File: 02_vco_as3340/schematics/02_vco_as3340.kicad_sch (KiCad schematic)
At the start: 52 parts, among them U1 AS3340, U2 TL074, U3 TL074

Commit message: worked on  02_vco_as3340 schematics
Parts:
- removed C2: 1nF, Capacitor_THT:C_Disc_D6.0mm_W2.5mm_P5.00mm, symbol Device:C_Small
- removed R16, R27: 1k, Resistor_THT:R_Axial_DIN0207_L6.3mm_D2.5mm_P10.16mm_Horizontal, symbol Device:R_Small
- removed R19, R20, R21: 47k, Resistor_THT:R_Axial_DIN0207_L6.3mm_D2.5mm_P10.16mm_Horizontal, symbol Device:R_Small
- removed R22: 2k, Resistor_THT:R_Axial_DIN0207_L6.3mm_D2.5mm_P10.16mm_Horizontal, symbol Device:R_Small
- removed R28, R29, R33, R6: 100k, Resistor_THT:R_Axial_DIN0207_L6.3mm_D2.5mm_P10.16mm_Horizontal, symbol Device:R_Small
- removed RV5: 100k, Potentiometer_THT:Potentiometer_Alpha_RD901F-40-00D_Single_Vertical_CircularHoles, symbol Device:R_Potentiometer_Small
- removed TP2: 10k, Potentiometer_THT:Potentiometer_Vishay_T73XW_Horizontal, symbol Device:R_Potentiometer_Trim
- removed unit 3 of U2
- removed unit 2 of U2
- removed unit 4 of U3
- removed unit 3 of U3
- removed ZD1: 10V Zener Diode, symbol Device:D_Zener_Small
- added C1001: 1nF, Capacitor_THT:C_Disc_D6.0mm_W2.5mm_P5.00mm, symbol Device:C_Small
- added R1001: 1k, Resistor_THT:R_Axial_DIN0207_L6.3mm_D2.5mm_P10.16mm_Horizontal, symbol Device:R_Small
- added R1002, R1009: 33k, Resistor_THT:R_Axial_DIN0207_L6.3mm_D2.5mm_P10.16mm_Horizontal, symbol Device:R_Small
- added R1003: 150k, Resistor_THT:R_Axial_DIN0207_L6.3mm_D2.5mm_P10.16mm_Horizontal, symbol Device:R_Small
- added R1004: 15k, Resistor_THT:R_Axial_DIN0207_L6.3mm_D2.5mm_P10.16mm_Horizontal, symbol Device:R_Small
- added R1005, R1007: 82k, Resistor_THT:R_Axial_DIN0207_L6.3mm_D2.5mm_P10.16mm_Horizontal, symbol Device:R_Small
- added R1006: 220k, Resistor_THT:R_Axial_DIN0207_L6.3mm_D2.5mm_P10.16mm_Horizontal, symbol Device:R_Small
- added R1008, R1010, R1011, R1012, R1014: 100k, Resistor_THT:R_Axial_DIN0207_L6.3mm_D2.5mm_P10.16mm_Horizontal, symbol Device:R_Small
- added R1013: 22k, Resistor_THT:R_Axial_DIN0207_L6.3mm_D2.5mm_P10.16mm_Horizontal, symbol Device:R_Small
- added RV1001: 100k, Potentiometer_THT:Potentiometer_Alpha_RD901F-40-00D_Single_Vertical_CircularHoles, symbol Device:R_Potentiometer_Small
- added TP1001, TP1002: 10k, Potentiometer_THT:Potentiometer_Vishay_T73XW_Horizontal, symbol Device:R_Potentiometer_Trim
- R31: value 100k -> 47k
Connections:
- net PWM is gone; now on an unnamed net: U1.5 (VPWM)
- net +12V: now also TP1.3, R1003.1, R1010.1, R1014.1; no longer TP1.1
- net -12V: now also R1006.2
- net GNDREF: now also C1001.1, R1004.2, R1009.2, R1013.2, RV1001.3; no longer RV4.3, U2.12 (+)
- net Triangle Wave OUT: now also R1001.2
- net at U2.3 (+): now also R1009.1, R1010.2
- net at U1.10 (VTO): now also R1002.2; no longer U3.5 (+)
- net at U1.11 (CAP): now also C1001.2
- net at R2.1, R23.1, R24.2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: now also TP1002.1, TP1002.2
- net at U1.4 (VP): now also R1008.1
- net at U1.8 (VSO): now also R1011.1; no longer U3.3 (+)
- net at R1.1: now also TP1002.3
- net at U3.6 (-): now also R1002.1, R1005.1; no longer U3.7
- net at R25.1, U2.1: now also R1007.2; no longer U2.2 (-)
- net at R17.1, U3.1: now also R1012.2; no longer U3.2 (-)
- net at RV4.2: now also U2.12 (+)
- net at R4.2, TP1.2: now also TP1.1; no longer TP1.3
- net PWM IN: no longer names the net of R32.1
- net PWM IN: now also RV1001.2
- new net: R1007.1, R1008.2, U2.2 (-)
- new net: R1004.1, TP1001.1
- new net: R1003.2, TP1001.2, TP1001.3, U3.5 (+)
- new net: R1001.1, R1005.2, U3.7
- new net: R1013.1, R1014.2, U3.3 (+)
- new net: R1011.2, R1012.1, U3.2 (-)
- new net: R1006.1, RV4.3
- new net PWM  CV IN: RV1001.1
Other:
- moved on the sheet: C10, C4, C5, C6, C8, C9, D1, D2, R10, R11, R12, R13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

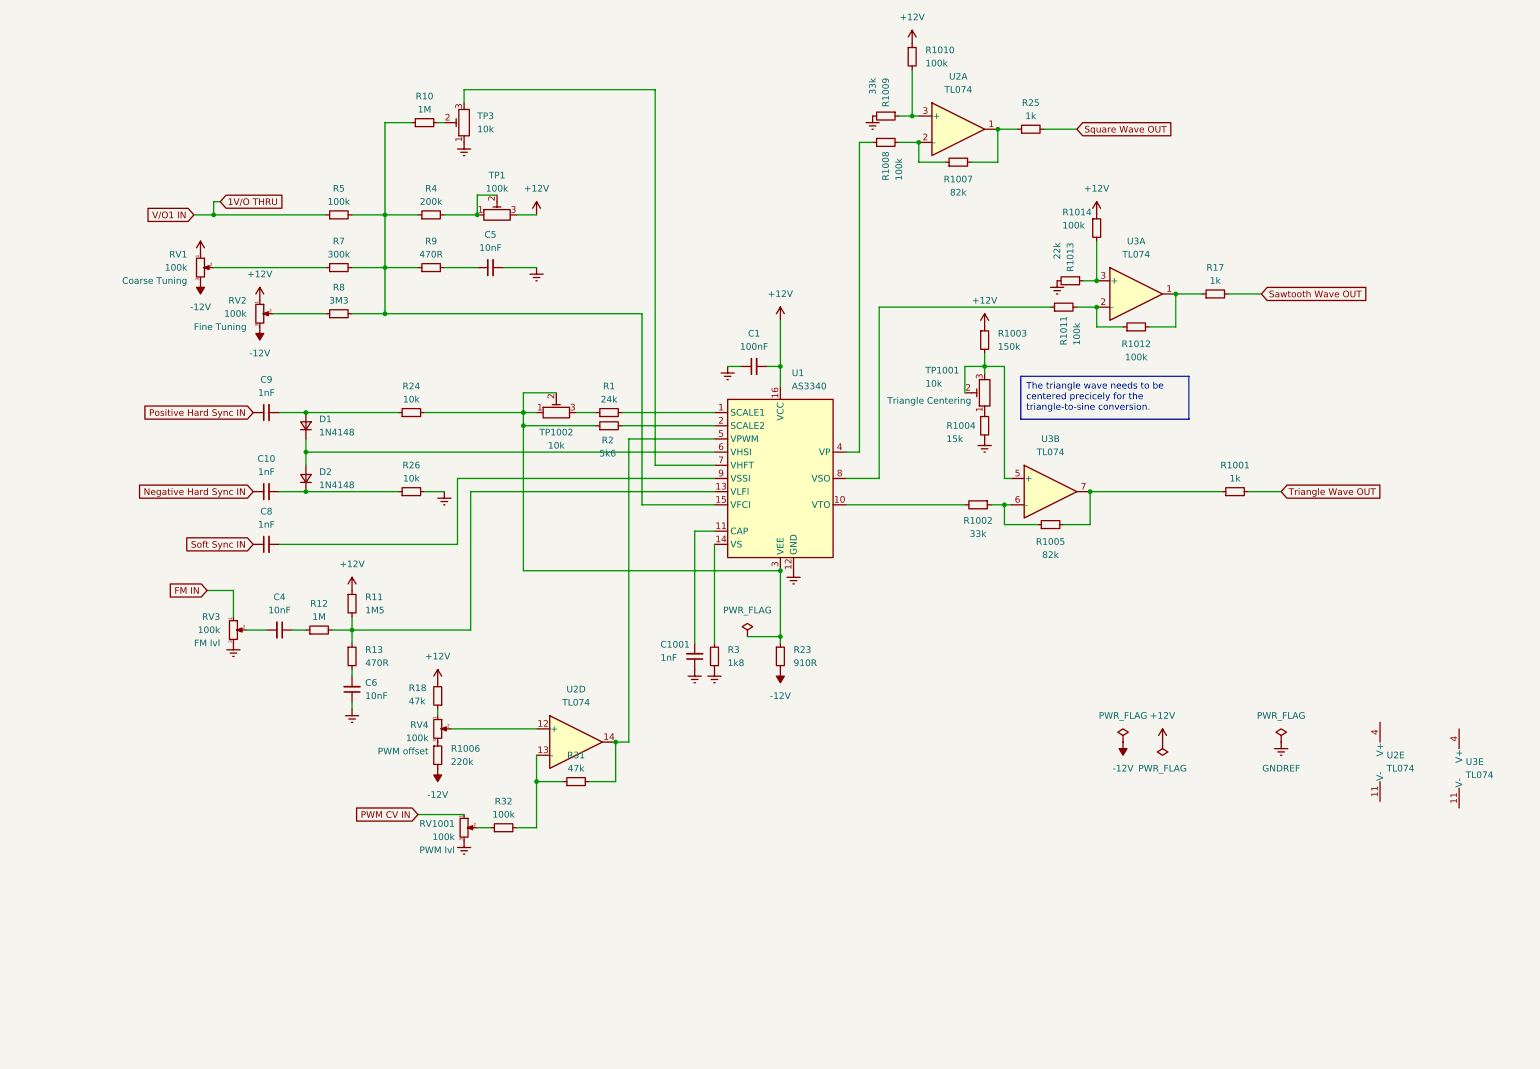
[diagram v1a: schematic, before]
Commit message: added 03_env_pluck
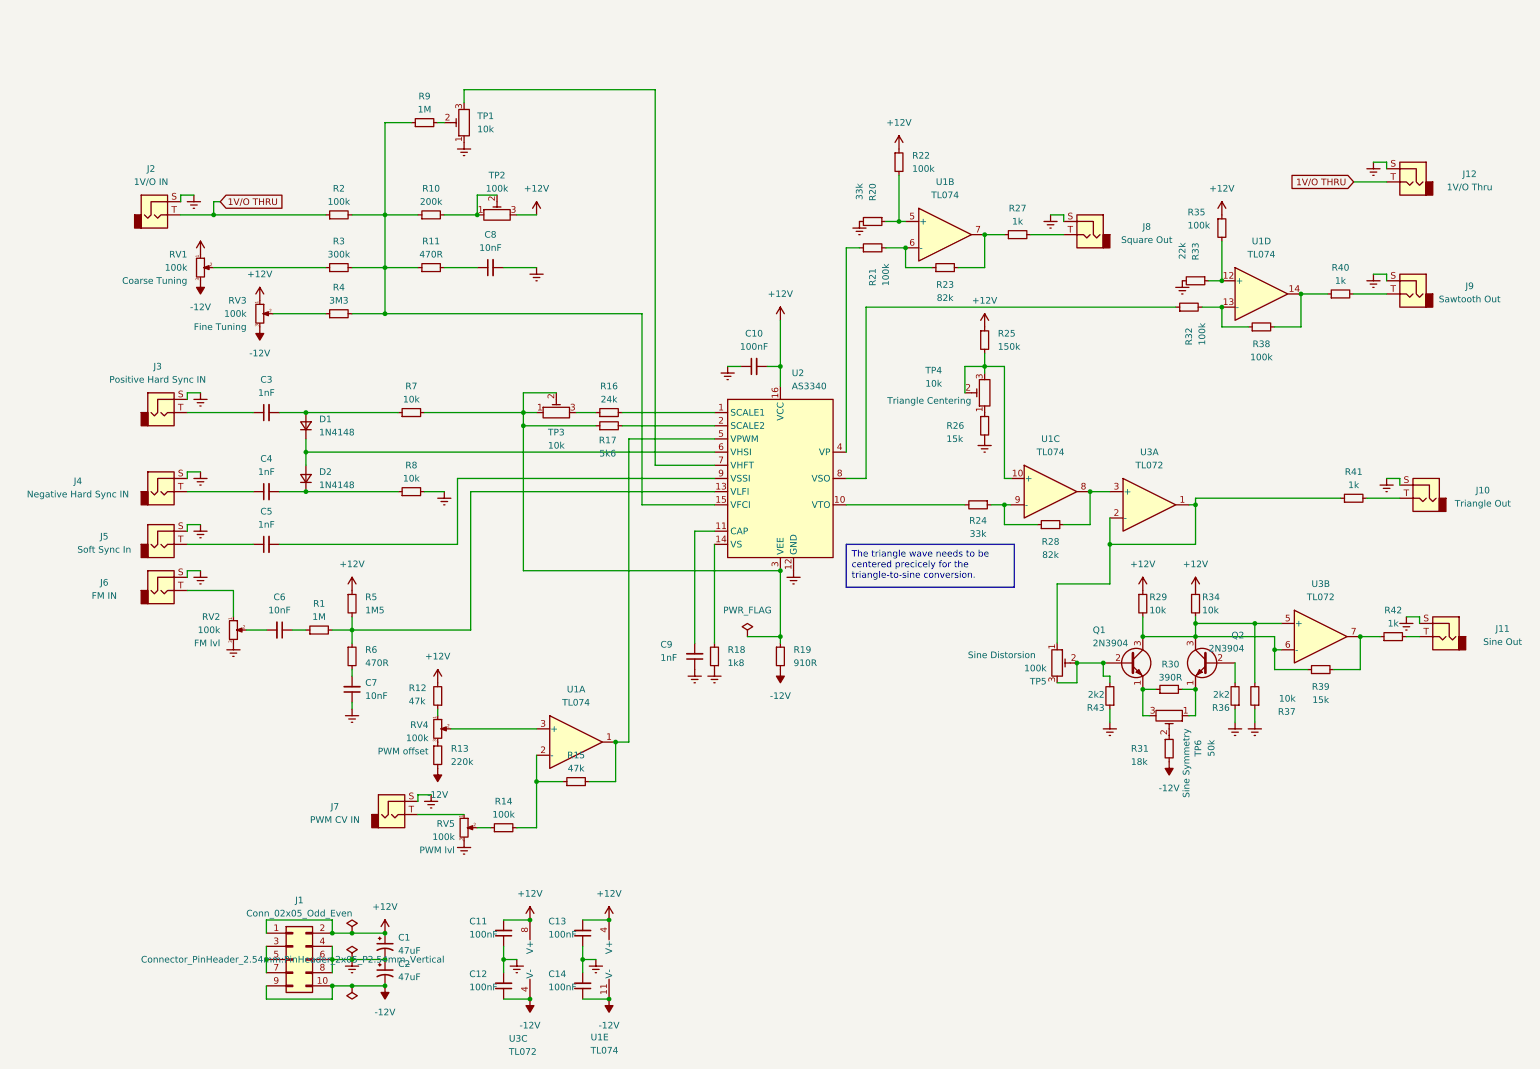
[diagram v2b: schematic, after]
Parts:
- removed U2, U3: TL074, Package_DIP:DIP-14_W7.62mm, symbol Amplifier_Operational:TL074
- added C1, C2: 47uF, Capacitor_THT:CP_Radial_D6.3mm_P2.50mm, symbol Device:C_Polarized_Small_US
- added C11, C12, C13, C14: 100nF, Capacitor_THT:C_Disc_D6.0mm_W2.5mm_P5.00mm, symbol Device:C_Small
- added J1: Conn_02x05_Odd_Even, Connector_PinHeader_2.54mm:PinHeader_2x05_P2.54mm_Vertical, symbol Connector_Generic:Conn_02x05_Odd_Even
- added J10: Triangle Out, Connector_Audio:Jack_6.35mm_Neutrik_NJ5FD-V_Vertical, symbol Connector_Audio:AudioJack2
- added J11: Sine Out, Connector_Audio:Jack_6.35mm_Neutrik_NJ5FD-V_Vertical, symbol Connector_Audio:AudioJack2
- added J12: 1V/O Thru, Connector_Audio:Jack_6.35mm_Neutrik_NJ5FD-V_Vertical, symbol Connector_Audio:AudioJack2
- added J2: 1V/O IN, Connector_Audio:Jack_6.35mm_Neutrik_NJ5FD-V_Vertical, symbol Connector_Audio:AudioJack2
- added J3: Positive Hard Sync IN, Connector_Audio:Jack_6.35mm_Neutrik_NJ5FD-V_Vertical, symbol Connector_Audio:AudioJack2
- added J4: Negative Hard Sync IN, Connector_Audio:Jack_6.35mm_Neutrik_NJ5FD-V_Vertical, symbol Connector_Audio:AudioJack2
- added J5: Soft Sync In, Connector_Audio:Jack_6.35mm_Neutrik_NJ5FD-V_Vertical, symbol Connector_Audio:AudioJack2
- added J6: FM IN, Connector_Audio:Jack_6.35mm_Neutrik_NJ5FD-V_Vertical, symbol Connector_Audio:AudioJack2
- added J7: PWM CV IN, Connector_Audio:Jack_6.35mm_Neutrik_NJ5FD-V_Vertical, symbol Connector_Audio:AudioJack2
- added J8: Square Out, Connector_Audio:Jack_6.35mm_Neutrik_NJ5FD-V_Vertical, symbol Connector_Audio:AudioJack2
- added J9: Sawtooth Out, Connector_Audio:Jack_6.35mm_Neutrik_NJ5FD-V_Vertical, symbol Connector_Audio:AudioJack2
- added Q1, Q2: 2N3904, Package_TO_SOT_THT:TO-92_Inline, symbol Transistor_BJT:2N3904
- added R29, R34, R37: 10k, Resistor_THT:R_Axial_DIN0207_L6.3mm_D2.5mm_P10.16mm_Horizontal, symbol Device:R_Small
- added R30: 390R, Resistor_THT:R_Axial_DIN0207_L6.3mm_D2.5mm_P10.16mm_Horizontal, symbol Device:R_Small
- added R31: 18k, Resistor_THT:R_Axial_DIN0207_L6.3mm_D2.5mm_P10.16mm_Horizontal, symbol Device:R_Small
- added R36, R43: 2k2, Resistor_THT:R_Axial_DIN0207_L6.3mm_D2.5mm_P10.16mm_Horizontal, symbol Device:R_Small
- added R39: 15k, Resistor_THT:R_Axial_DIN0207_L6.3mm_D2.5mm_P10.16mm_Horizontal, symbol Device:R_Small
- added R42: 1k, Resistor_THT:R_Axial_DIN0207_L6.3mm_D2.5mm_P10.16mm_Horizontal, symbol Device:R_Small
- added TP5: 100k, Potentiometer_THT:Potentiometer_Vishay_T73XW_Horizontal, symbol Device:R_Potentiometer_Trim
- added TP6: 50k, Potentiometer_THT:Potentiometer_Vishay_T73XW_Horizontal, symbol Device:R_Potentiometer_Trim
- added U1: TL074, Package_DIP:DIP-14_W10.16mm, symbol Amplifier_Operational:TL074
- added U3: TL072, Package_DIP:DIP-8_W10.16mm, symbol Amplifier_Operational:TL072
- renumbered C1 to C10, C9 to C3, C10 to C4, C8 to C5, C4 to C6, C6 to C7, C5 to C8, C1001 to C9, R12 to R1, R4 to R10, R9 to R11, R18 to R12, R1006 to R13, R32 to R14, R31 to R15, R1 to R16, R2 to R17, R3 to R18, R23 to R19, R5 to R2, R1009 to R20, R1008 to R21, R1010 to R22, R1007 to R23, R1002 to R24, R1003 to R25, R1004 to R26, R25 to R27, R1005 to R28, R7 to R3, R1011 to R32, R1013 to R33, R1014 to R35, R1012 to R38, R8 to R4, R17 to R40, R1001 to R41, R11 to R5, R13 to R6, R24 to R7, R26 to R8, R10 to R9, RV3 to RV2, RV2 to RV3, RV1001 to RV5, TP3 to TP1, TP1 to TP2, TP1002 to TP3, TP1001 to TP4, U1 to U2
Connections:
- net +12V: now also C1.1, C11.2, C13.2, J1.1 (Pin_1), J1.2 (Pin_2), R29.1, R34.1, U1.4 (V+), U3.8 (V+)
- net -12V: now also C12.1, C14.1, C2.2, J1.10 (Pin_10), J1.9 (Pin_9), R31.2, U1.11 (V-), U3.4 (V-)
- net 1V/O THRU: now also J12.T, J2.T
- net GNDREF: now also C1.2, C11.1, C12.2, C13.1, C14.2, C2.1, J1.4 (Pin_4), J1.6 (Pin_6), J1.8 (Pin_8), J10.S, J11.S, J12.S, J2.S, J3.S, J4.S, J5.S, J6.S, J7.S, J8.S, J9.S, R36.1, R37.1, R43.1
- net at R21.2, R23.1: now also U1.6 (-)
- net at R24.1, R28.1: now also U1.9 (-)
- net at R15.2, U2.5 (VPWM): now also U1.1
- net at R20.1, R22.2: now also U1.5 (+)
- net at R25.2, TP4.2, TP4.3: now also U1.10 (+)
- net at R28.2: now also U1.8, U3.3 (+); no longer R41.1
- net at R23.2, R27.1: now also U1.7
- net at RV4.2: now also U1.3 (+)
- net at R14.2, R15.1: now also U1.2 (-)
- net at R33.1, R35.2: now also U1.12 (+)
- net at R32.2, R38.1: now also U1.13 (-)
- net at R38.2, R40.1: now also U1.14
- net FM IN: no longer names the net of RV2.1
- net FM IN: now also J6.T
- net Negative Hard Sync IN: no longer names the net of C4.1
- net Negative Hard Sync IN: now also J4.T
- net PWM  CV IN: no longer names the net of RV5.1
- net PWM  CV IN: now also J7.T
- net Positive Hard Sync IN: no longer names the net of C3.1
- net Positive Hard Sync IN: now also J3.T
- net Sawtooth Wave OUT: no longer names the net of R40.2
- net Sawtooth Wave OUT: now also J9.T
- net Soft Sync IN: no longer names the net of C5.1
- net Soft Sync IN: now also J5.T
- net Square Wave OUT: no longer names the net of R27.2
- net Square Wave OUT: now also J8.T
- net Triangle Wave OUT: no longer names the net of R41.2
- net Triangle Wave OUT: now also J10.T
- new net: R39.2, R42.1, U3.7
- new net: J11.T, R42.2
- new net: J1.3 (Pin_3), J1.5 (Pin_5), J1.7 (Pin_7)
- new net: Q2.1 (E), R30.2, TP6.1
- new net: R31.1, TP6.2
- new net: Q1.1 (E), R30.1, TP6.3
- new net: Q1.3 (C), Q2.3 (C), R29.2, R34.2, R37.2, R39.1, U3.5 (+), U3.6 (-)
- new net: Q2.2 (B), R36.2
- new net: Q1.2 (B), R43.2, TP5.2, TP5.3
- new net: R41.1, TP5.1, U3.1, U3.2 (-)
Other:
- moved on the sheet: R20, R21, R22, R23, R27, R32, R33, R35, R38, R40, R41
